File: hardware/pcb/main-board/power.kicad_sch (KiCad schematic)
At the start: 20 parts, among them Q501 DMG2302U, SW501 NO POP, SW502 NO POP, U501 PT4110, U502 AZ1117H-3.3_SOT223

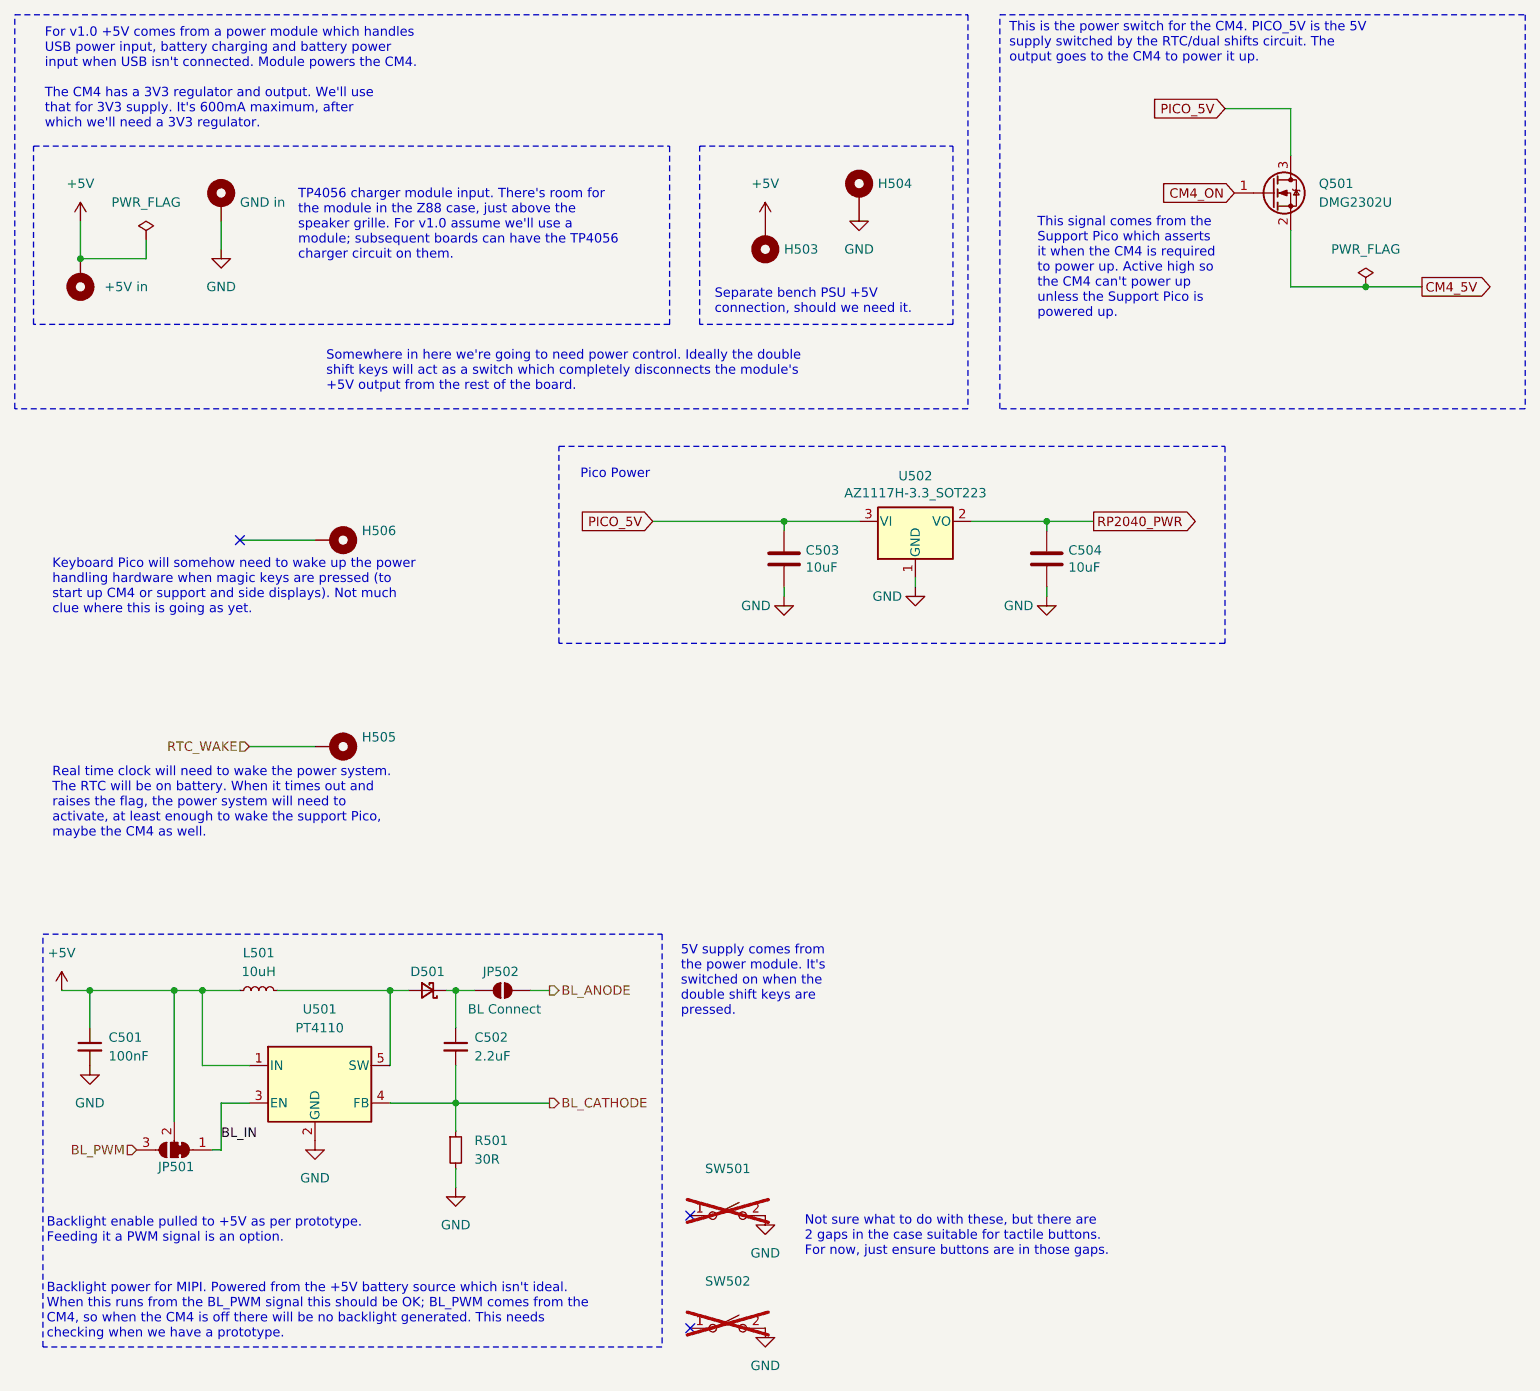
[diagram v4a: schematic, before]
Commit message: start the support pico rp2040 replacement
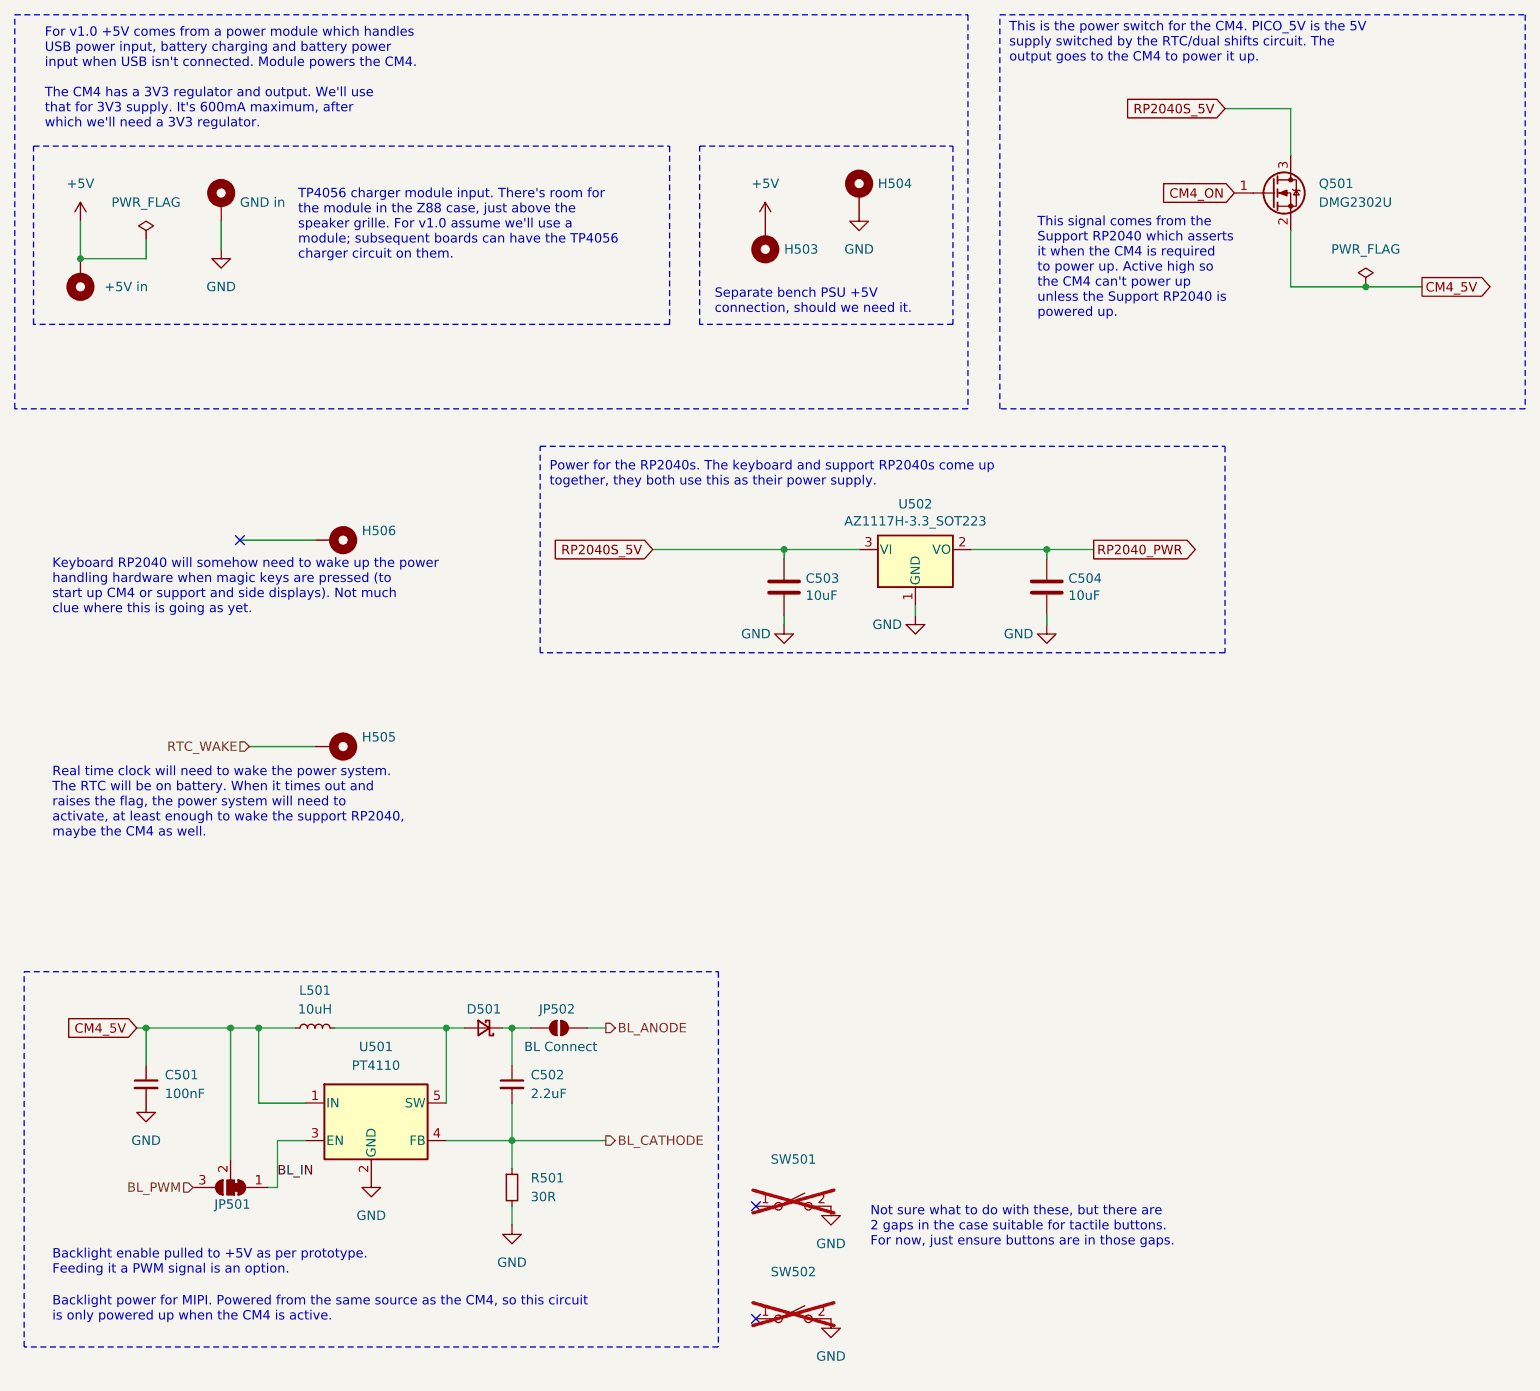
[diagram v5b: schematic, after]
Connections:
- net +5V: no longer C501.1, JP501.2 (C), L501.1, U501.1 (IN)
- net CM4_5V: now also C501.1, JP501.2 (C), L501.1, U501.1 (IN)
- net PICO_5V renamed RP2040S_5V
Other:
- note added: "Backlight power for MIPI. Powered from the same source as the CM4, so this circuit is only powered up when the CM4 is active."
- note added: "Keyboard RP2040 will somehow need to wake up the power handling hardware when magic keys are pressed (to start up CM4 or support and side displays). Not much clue where this is going as yet."
- note added: "Power for the RP2040s. The keyboard and support RP2040s come up together, they both use this as their power supply."
- note added: "Real time clock will need to wake the power system. The RTC will be on battery. When it times out and raises the flag, the power system will need to activate, at least enough to wake the support RP2040, maybe the CM4 as well."
- note added: "This signal comes from the Support RP2040 which asserts it when the CM4 is required to power up. Active high so the CM4 can't power up unless the Support RP2040 is powered up."
- note removed: "5V supply comes from the power module. It's switched on when the double shift keys are pressed."
- note removed: "Backlight power for MIPI. Powered from the +5V battery source which isn't ideal. When this runs from the BL_PWM signal this should be OK; BL_PWM comes from the CM4, so when the CM4 is off there will be no backlight generated. This needs checking when we have a prototype."
- note removed: "Keyboard Pico will somehow need to wake up the power handling hardware when magic keys are pressed (to start up CM4 or support and side displays). Not much clue where this is going as yet."
- note removed: "Pico Power"
- note removed: "Real time clock will need to wake the power system. The RTC will be on battery. When it times out and raises the flag, the power system will need to activate, at least enough to wake the support Pico, maybe the CM4 as well."
- note removed: "Somewhere in here we're going to need power control. Ideally the double shift keys will act as a switch which completely disconnects the module's +5V output from the rest of the board."
- note removed: "This signal comes from the Support Pico which asserts it when the CM4 is required to power up. Active high so the CM4 can't power up unless the Support Pico is powered up."
- moved on the sheet: C501, C502, C503, C504, D501, JP501, JP502, L501, R501, SW501, SW502, U501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

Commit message: a few more tidyups, almost ready for dual shifts stuff now
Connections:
- net RP2040_PWR renamed RP2040_3V3_PWR
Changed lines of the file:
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@@
 	(rectangle
 		(start 83.82 72.39)
-		(end 176.53 100.33)
+		(end 179.07 100.33)
 		(stroke
 			(width 0)
@@
 		)
 	)
-	(global_label "RP2040_PWR"
+	(global_label "RP2040_3V3_PWR"
 		(shape output)
 		(at 158.75 86.36 0)

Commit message: more support rp2040 cleanups
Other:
- note added: "This is the power switch for the CM4. RP2040_5V is the 5V supply switched by the RTC/dual shifts circuit. The output goes to the CM4 to power it up."
- note removed: "This is the power switch for the CM4. PICO_5V is the 5V supply switched by the RTC/dual shifts circuit. The output goes to the CM4 to power it up."
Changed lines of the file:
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@@
 		)
 	)
-	(text "This is the power switch for the CM4. PICO_5V is the 5V\nsupply switched by the RTC/dual shifts circuit. The\noutput goes to the CM4 to power it up."
+	(text "This is the power switch for the CM4. RP2040_5V is the 5V\nsupply switched by the RTC/dual shifts circuit. The\noutput goes to the CM4 to power it up."
 		(exclude_from_sim no)
 		(at 147.32 17.78 0)
